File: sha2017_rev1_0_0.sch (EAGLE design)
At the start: 201 parts, among them IC1 CP210X_USB_UART, IC2 AP7215, IC3 ESP32WROOM32, IC4 TP4056, M1 MOTOR10MM, Q1 MMBT2222A, Q2 MMBT2222A, Q3 MMBT2222A, Q4 MMBT2222A, Q5 SI1304 BDL, Q6 MMBT2222A, T1 MOSFET-PCHANNEL, T2 MOSFET-PCHANNEL, T3 MOSFET-PCHANNEL, U1 MPR121QR2, X2 2908-05WB-MG, X4 JST-PH3

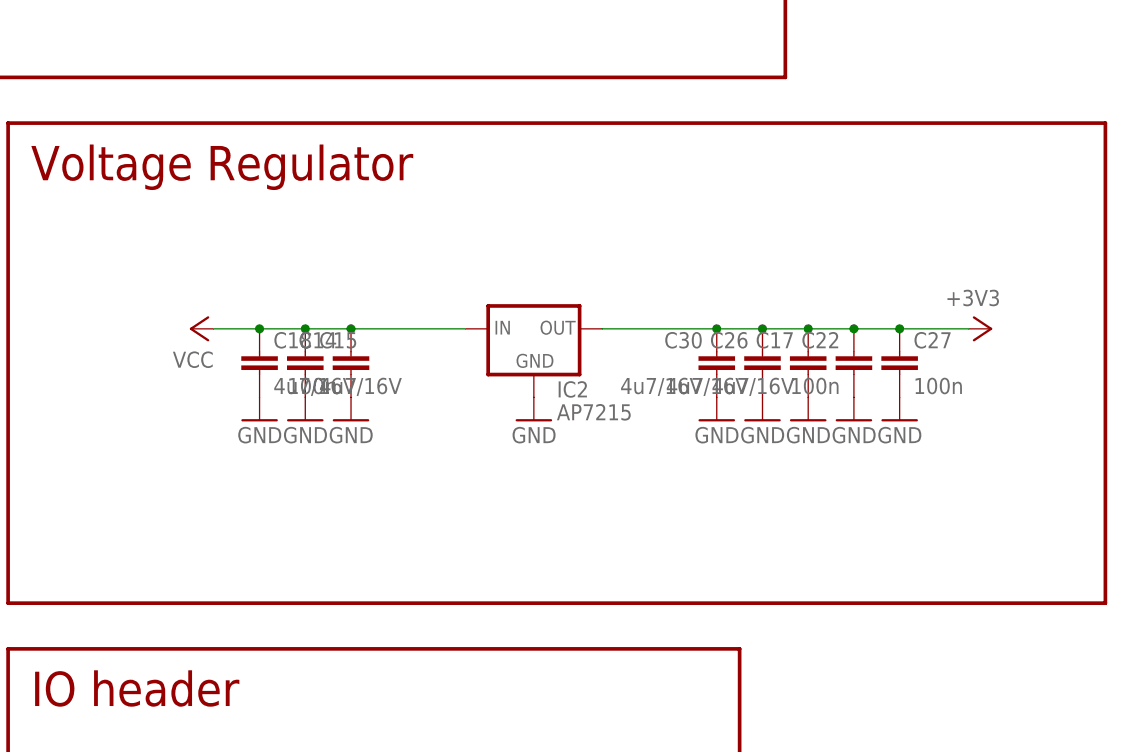
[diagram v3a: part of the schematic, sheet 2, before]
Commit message: Extra vreg (not routed\!)
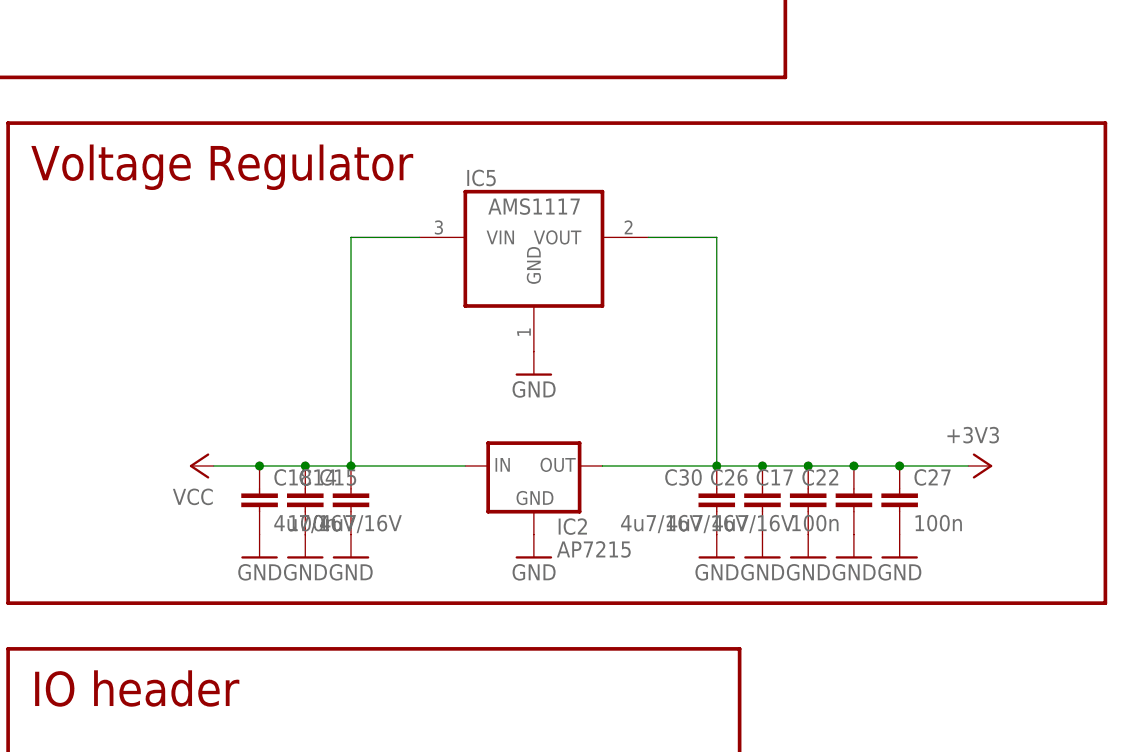
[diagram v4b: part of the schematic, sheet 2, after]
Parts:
- added IC5: AMS1117, burr-brown:REG1117
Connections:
- net +3V3: now also IC5.VOUT
- net GND: now also IC5.GND
- net VCC: now also IC5.VIN
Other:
- moved on the sheet: C14, C15, C17, C18, C22, C26, C27, C30, IC2
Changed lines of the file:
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@@
 <part name="+3V8" library="supply1" deviceset="+3V3" device=""/>
 <part name="GND55" library="supply1" deviceset="GND" device=""/>
+<part name="IC5" library="burr-brown" deviceset="REG1117" device="" value="AMS1117"/>
+<part name="GND58" library="supply1" deviceset="GND" device=""/>
 </parts>
 <sheets>
@@
 <instances>
 <instance part="FRAME4" gate="G$1" x="0" y="0"/>
-<instance part="C14" gate="G$1" x="274.32" y="146.05" rot="MR0">
-<attribute name="PARTNO" x="274.32" y="146.05" size="1.778" layer="96" rot="MR0" display="off"/>
-</instance>
-<instance part="C15" gate="G$1" x="269.24" y="147.32">
-<attribute name="PARTNO" x="269.24" y="147.32" size="1.778" layer="96" rot="MR0" display="off"/>
-</instance>
-<instance part="C17" gate="G$1" x="325.12" y="147.32" rot="MR0">
-<attribute name="PARTNO" x="325.12" y="147.32" size="1.778" layer="96" rot="MR0" display="off"/>
-</instance>
-<instance part="C22" gate="G$1" x="330.2" y="146.05" rot="MR0">
-<attribute name="PARTNO" x="330.2" y="146.05" size="1.778" layer="96" rot="MR0" display="off"/>
-</instance>
-<instance part="C27" gate="G$1" x="335.28" y="146.05">
-<attribute name="PARTNO" x="335.28" y="146.05" size="1.778" layer="96" rot="MR0" display="off"/>
-</instance>
-<instance part="GND20" gate="1" x="269.24" y="139.7" rot="MR0"/>
-<instance part="GND21" gate="1" x="274.32" y="139.7" rot="MR0"/>
-<instance part="GND22" gate="1" x="294.64" y="139.7" rot="MR0"/>
-<instance part="GND24" gate="1" x="325.12" y="139.7" rot="MR0"/>
-<instance part="GND25" gate="1" x="330.2" y="139.7" rot="MR0"/>
-<instance part="GND27" gate="1" x="335.28" y="139.7" rot="MR0"/>
-<instance part="+3V2" gate="G$1" x="345.44" y="149.86" rot="R270"/>
-<instance part="C26" gate="G$1" x="320.04" y="147.32" rot="MR0">
-<attribute name="PARTNO" x="320.04" y="147.32" size="1.778" layer="96" rot="MR0" display="off"/>
-</instance>
-<instance part="C30" gate="G$1" x="314.96" y="147.32" rot="MR0">
-<attribute name="PARTNO" x="314.96" y="147.32" size="1.778" layer="96" rot="MR0" display="off"/>
-</instance>
-<instance part="GND28" gate="1" x="320.04" y="139.7" rot="MR0"/>
-<instance part="GND29" gate="1" x="314.96" y="139.7" rot="MR0"/>
-<instance part="IC2" gate="G$1" x="294.64" y="149.86">
-<attribute name="PARTNO" x="294.64" y="149.86" size="1.778" layer="96" rot="MR0" display="off"/>
-</instance>
-<instance part="C18" gate="G$1" x="264.16" y="147.32">
-<attribute name="PARTNO" x="264.16" y="147.32" size="1.778" layer="96" rot="MR0" display="off"/>
-</instance>
-<instance part="GND14" gate="1" x="264.16" y="139.7" rot="MR0"/>
+<instance part="C14" gate="G$1" x="274.32" y="130.81" rot="MR0">
+<attribute name="PARTNO" x="274.32" y="130.81" size="1.778" layer="96" rot="MR0" display="off"/>
+</instance>
+<instance part="C15" gate="G$1" x="269.24" y="132.08">
+<attribute name="PARTNO" x="269.24" y="132.08" size="1.778" layer="96" rot="MR0" display="off"/>
+</instance>
+<instance part="C17" gate="G$1" x="325.12" y="132.08" rot="MR0">
+<attribute name="PARTNO" x="325.12" y="132.08" size="1.778" layer="96" rot="MR0" display="off"/>
+</instance>
+<instance part="C22" gate="G$1" x="330.2" y="130.81" rot="MR0">
+<attribute name="PARTNO" x="330.2" y="130.81" size="1.778" layer="96" rot="MR0" display="off"/>
+</instance>
+<instance part="C27" gate="G$1" x="335.28" y="130.81">
+<attribute name="PARTNO" x="335.28" y="130.81" size="1.778" layer="96" rot="MR0" display="off"/>
+</instance>
+<instance part="GND20" gate="1" x="269.24" y="124.46" rot="MR0"/>
+<instance part="GND21" gate="1" x="274.32" y="124.46" rot="MR0"/>
+<instance part="GND22" gate="1" x="294.64" y="124.46" rot="MR0"/>
+<instance part="GND24" gate="1" x="325.12" y="124.46" rot="MR0"/>
+<instance part="GND25" gate="1" x="330.2" y="124.46" rot="MR0"/>
+<instance part="GND27" gate="1" x="335.28" y="124.46" rot="MR0"/>
+<instance part="+3V2" gate="G$1" x="345.44" y="134.62" rot="R270"/>
+<instance part="C26" gate="G$1" x="320.04" y="132.08" rot="MR0">
+<attribute name="PARTNO" x="320.04" y="132.08" size="1.778" layer="96" rot="MR0" display="off"/>
+</instance>
+<instance part="C30" gate="G$1" x="314.96" y="132.08" rot="MR0">
+<attribute name="PARTNO" x="314.96" y="132.08" size="1.778" layer="96" rot="MR0" display="off"/>
+</instance>
+<instance part="GND28" gate="1" x="320.04" y="124.46" rot="MR0"/>
+<instance part="GND29" gate="1" x="314.96" y="124.46" rot="MR0"/>
+<instance part="IC2" gate="G$1" x="294.64" y="134.62">
+<attribute name="PARTNO" x="294.64" y="134.62" size="1.778" layer="96" rot="MR0" display="off"/>
+</instance>
+<instance part="C18" gate="G$1" x="264.16" y="132.08">
+<attribute name="PARTNO" x="264.16" y="132.08" size="1.778" layer="96" rot="MR0" display="off"/>
+</instance>
+<instance part="GND14" gate="1" x="264.16" y="124.46" rot="MR0"/>
 <instance part="F2" gate="G$1" x="92.71" y="144.78" rot="R90">
 <attribute name="PARTNO" x="92.71" y="144.78" size="5.08" layer="96" rot="R90" display="off"/>
@@
 <attribute name="PARTNO" x="35.56" y="144.78" size="5.08" layer="96" display="off"/>
 </instance>
-<instance part="P+1" gate="VCC" x="256.54" y="149.86" rot="R90"/>
+<instance part="P+1" gate="VCC" x="256.54" y="134.62" rot="R90"/>
 <instance part="C24" gate="G$1" x="210.82" y="142.24" rot="MR0">
 <attribute name="PARTNO" x="210.82" y="142.24" size="1.778" layer="96" display="off"/>
@@
 </instance>
 <instance part="GND55" gate="1" x="264.16" y="68.58" rot="MR0"/>
+<instance part="IC5" gate="G$1" x="294.64" y="160.02"/>
+<instance part="GND58" gate="1" x="294.64" y="144.78" rot="MR0"/>
 </instances>
 <busses>
@@
 <wire x1="264.16" y1="86.36" x2="264.16" y2="71.12" width="0.1524" layer="91"/>
 </segment>
+<segment>
+<pinref part="IC5" gate="G$1" pin="GND"/>
+<pinref part="GND58" gate="1" pin="GND"/>
+</segment>
 </net>
 <net name="+3V3" class="0">
@@
 <pinref part="+3V2" gate="G$1" pin="+3V3"/>
 <pinref part="C17" gate="G$1" pin="1"/>
-<junction x="325.12" y="149.86"/>
-<wire x1="314.96" y1="149.86" x2="320.04" y2="149.86" width="0.1524" layer="91"/>
-<wire x1="320.04" y1="149.86" x2="325.12" y2="149.86" width="0.1524" layer="91"/>
-<wire x1="325.12" y1="149.86" x2="330.2" y2="149.86" width="0.1524" layer="91"/>
+<junction x="325.12" y="134.62"/>
+<wire x1="314.96" y1="134.62" x2="320.04" y2="134.62" width="0.1524" layer="91"/>
+<wire x1="320.04" y1="134.62" x2="325.12" y2="134.62" width="0.1524" layer="91"/>
+<wire x1="325.12" y1="134.62" x2="330.2" y2="134.62" width="0.1524" layer="91"/>
 <pinref part="C22" gate="G$1" pin="1"/>
-<junction x="330.2" y="149.86"/>
-<wire x1="330.2" y1="149.86" x2="335.28" y2="149.86" width="0.1524" layer="91"/>
+<junction x="330.2" y="134.62"/>
+<wire x1="330.2" y1="134.62" x2="335.28" y2="134.62" width="0.1524" layer="91"/>
 <pinref part="C27" gate="G$1" pin="1"/>
-<junction x="335.28" y="149.86"/>
-<wire x1="335.28" y1="149.86" x2="342.9" y2="149.86" width="0.1524" layer="91"/>
+<junction x="335.28" y="134.62"/>
+<wire x1="335.28" y1="134.62" x2="342.9" y2="134.62" width="0.1524" layer="91"/>
 <pinref part="C26" gate="G$1" pin="1"/>
-<junction x="320.04" y="149.86"/>
+<junction x="320.04" y="134.62"/>
 <pinref part="C30" gate="G$1" pin="1"/>
-<junction x="314.96" y="149.86"/>
+<junction x="314.96" y="134.62"/>
 <pinref part="IC2" gate="G$1" pin="OUT"/>
-<wire x1="302.26" y1="149.86" x2="314.96" y2="149.86" width="0.1524" layer="91"/>
+<wire x1="302.26" y1="134.62" x2="314.96" y2="134.62" width="0.1524" layer="91"/>
+<pinref part="IC5" gate="G$1" pin="VOUT"/>
+<wire x1="307.34" y1="160.02" x2="314.96" y2="160.02" width="0.1524" layer="91"/>
+<wire x1="314.96" y1="160.02" x2="314.96" y2="134.62" width="0.1524" layer="91"/>
 </segment>
 <segment>
@@
 </segment>
 <segment>
-<wire x1="287.02" y1="149.86" x2="274.32" y2="149.86" width="0.1524" layer="91"/>
+<wire x1="287.02" y1="134.62" x2="274.32" y2="134.62" width="0.1524" layer="91"/>
 <pinref part="C14" gate="G$1" pin="1"/>
-<wire x1="274.32" y1="149.86" x2="269.24" y2="149.86" width="0.1524" layer="91"/>
-<junction x="274.32" y="149.86"/>
+<wire x1="274.32" y1="134.62" x2="269.24" y2="134.62" width="0.1524" layer="91"/>
+<junction x="274.32" y="134.62"/>
 <pinref part="C15" gate="G$1" pin="1"/>
-<wire x1="269.24" y1="149.86" x2="264.16" y2="149.86" width="0.1524" layer="91"/>
-<junction x="269.24" y="149.86"/>
+<wire x1="269.24" y1="134.62" x2="264.16" y2="134.62" width="0.1524" layer="91"/>
+<junction x="269.24" y="134.62"/>
 <pinref part="IC2" gate="G$1" pin="IN"/>
 <pinref part="C18" gate="G$1" pin="1"/>
-<junction x="264.16" y="149.86"/>
+<junction x="264.16" y="134.62"/>
 <pinref part="P+1" gate="VCC" pin="VCC"/>
-<wire x1="259.08" y1="149.86" x2="264.16" y2="149.86" width="0.1524" layer="91"/>
-</segment>
-<segment>
+<wire x1="259.08" y1="134.62" x2="264.16" y2="134.62" width="0.1524" layer="91"/>
+<pinref part="IC5" gate="G$1" pin="VIN"/>
+<wire x1="281.94" y1="160.02" x2="274.32" y2="160.02" width="0.1524" layer="91"/>
+<wire x1="274.32" y1="160.02" x2="274.32" y2="134.62" width="0.1524" layer="91"/>
+</segment>
+<segment>

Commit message: Replace vreg
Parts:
- removed IC5: AMS1117, burr-brown:REG1117
- IC2: value AP7215 -> LD117AS33TR; device badge:AP7215 -> v-reg:LD117AS33TR
- R2: device resistor:R-EU_R1206 -> rcl:R-EU_R1206
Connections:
- net +3V3: no longer IC5.VOUT
- net GND: now also IC2.ADJ; no longer IC2.GND, IC5.GND
- net VCC: no longer IC5.VIN
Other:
- moved on the sheet: C14, C15, C17, C18, C22, C26, C27, C30, IC2
